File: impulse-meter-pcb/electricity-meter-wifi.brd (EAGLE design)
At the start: 34.3 x 68.8 mm, 14 parts, among them U2 MCP1316MT-29ME/OT, U3 FM25L16B

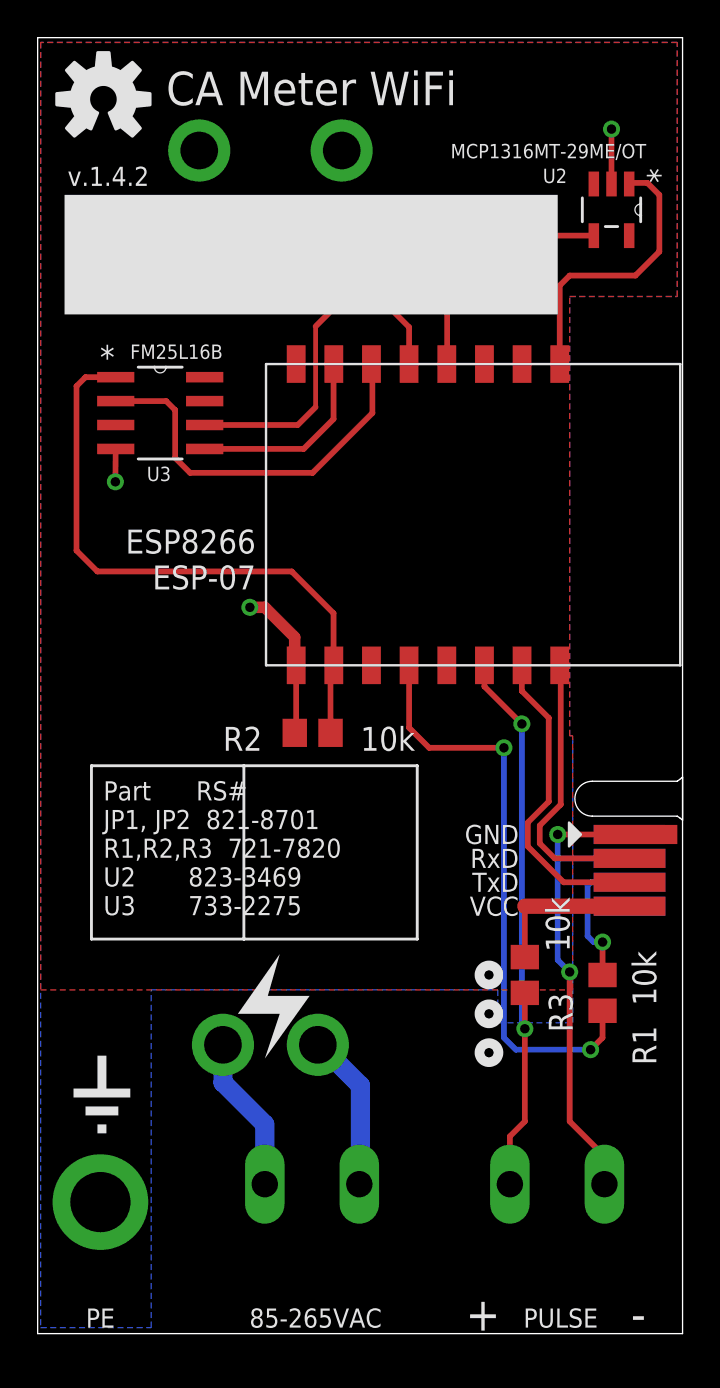
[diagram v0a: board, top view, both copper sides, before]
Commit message: added pull up resistor on GPIO02
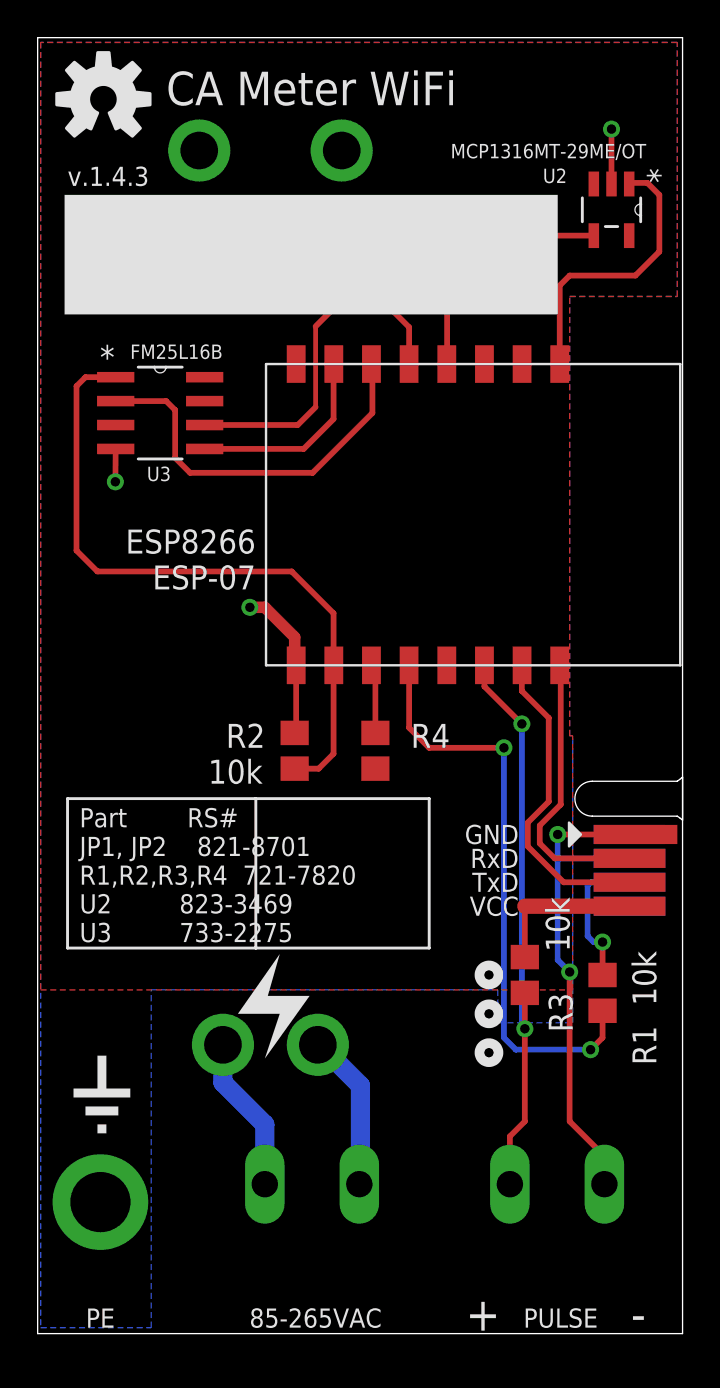
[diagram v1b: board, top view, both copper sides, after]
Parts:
- added R4: 10k, rcl:R0805
- moved R2 1.35 mm to (13.7, 31.0), turned to 270 degrees
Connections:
- new net N$14: ESP8266_ESP-07.GPIO2, R4.2
- net 3.3V: now also R4.1
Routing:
- net N$7: track 32.5 -> 36.2 mm
- net N$14: track 0.00 -> 3.68 mm
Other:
- board text added: "Part RS# JP1, JP2 821-8701 R1,R2,R3,R4 721-7820 U2 823-3469 U3 733-2275"
- board text added: "v.1.4.3"
- board text removed: "Part RS# JP1, JP2 821-8701 R1,R2,R3 721-7820 U2 823-3469 U3 733-2275"
- board text removed: "v.1.4.2"
